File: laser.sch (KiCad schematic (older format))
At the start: 1 part, among them U101 281698-3

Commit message: pushing other ports
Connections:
- net NewBoardCurrentControl/MODULATION_SIGNAL is gone; now on net ArduinoNano/5V_Power_Source: U101.3
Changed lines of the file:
@@
 $EndComp
 Wire Wire Line
-	2950 2550 3000 2550
+	2950 2550 3100 2550
 Wire Wire Line
-	3000 2550 3000 2150
+	3100 2550 3100 3750
 Wire Wire Line
-	3000 2150 10000 2150
+	3100 3750 10000 3750
 Wire Wire Line
-	10000 2150 10000 2800
+	10000 3750 10000 2900
+Connection ~ 10000 2900
+Wire Wire Line
+	10000 2900 10000 2800
 $EndSCHEMATC

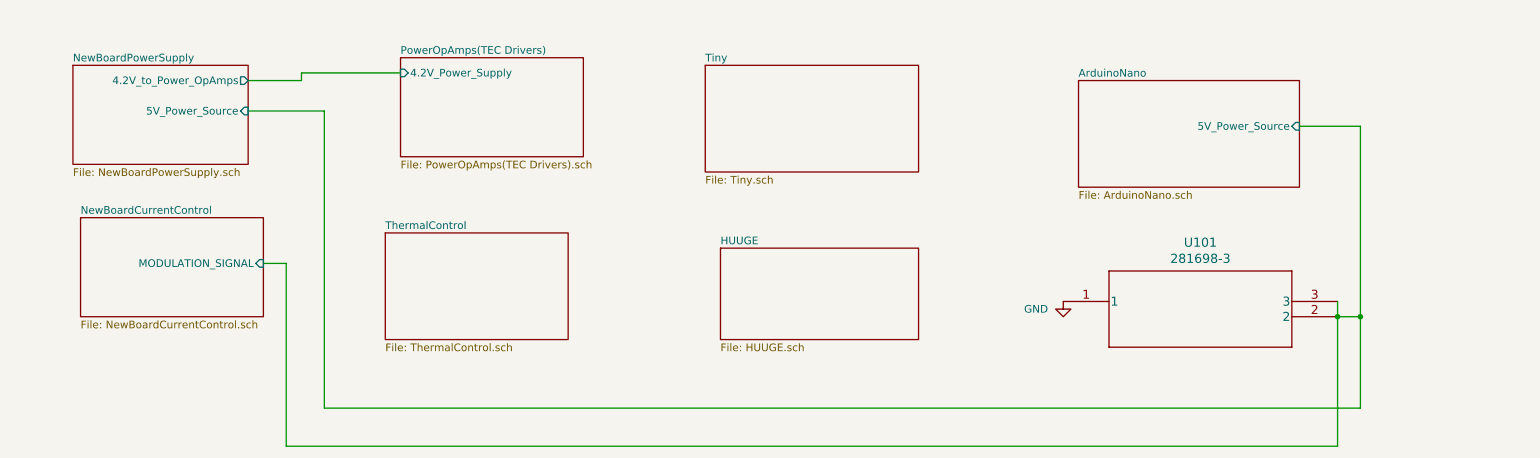
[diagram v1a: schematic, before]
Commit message: added other ports
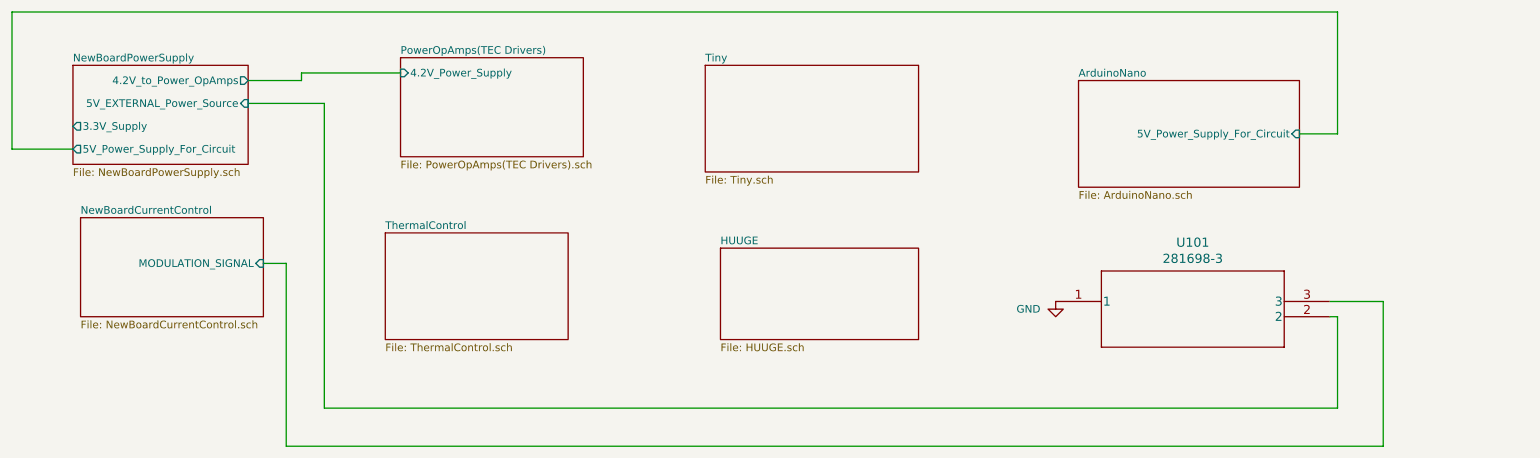
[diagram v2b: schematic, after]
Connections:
- net ArduinoNano/5V_Power_Source renamed NewBoardCurrentControl/MODULATION_SIGNAL
- net NewBoardCurrentControl/MODULATION_SIGNAL: no longer U101.2
- new net NewBoardPowerSupply/5V_EXTERNAL_Power_Source: U101.2
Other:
- moved on the sheet: U101
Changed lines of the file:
@@
 F1 "NewBoardPowerSupply.sch" 50
 F2 "4.2V_to_Power_OpAmps" O R 2850 1350 50
-F3 "5V_Power_Source" I R 2850 1550 50
+F3 "5V_EXTERNAL_Power_Source" I R 2850 1500 50
+F4 "3.3V_Supply" O L 1700 1650 50
+F5 "5V_Power_Supply_For_Circuit" O L 1700 1800 50
 $EndSheet
 $Sheet
@@
 F0 "ArduinoNano" 50
 F1 "ArduinoNano.sch" 50
-F2 "5V_Power_Source" I R 9750 1650 50
+F2 "5V_Power_Supply_For_Circuit" I R 9750 1700 50
 $EndSheet
 Wire Wire Line
@@
 L 3PinHeader:281698-3 U101
 U 1 1 60DB4391
-P 8200 2800
-F 0 "U101" H 9100 3187 60  0000 C CNN
-F 1 "281698-3" H 9100 3081 60  0000 C CNN
-F 2 "footprint libraries:281698-3" H 9100 3040 60  0001 C CNN
-F 3 "" H 8200 2800 60  0000 C CNN
-	1    8200 2800
+P 8150 2800
+F 0 "U101" H 9050 3187 60  0000 C CNN
+F 1 "281698-3" H 9050 3081 60  0000 C CNN
+F 2 "footprint libraries:281698-3" H 9050 3040 60  0001 C CNN
+F 3 "" H 8150 2800 60  0000 C CNN
+	1    8150 2800
 	1    0    0    -1
 $EndComp
 Wire Wire Line
-	2850 1550 3350 1550
+	10000 2900 9950 2900
 Wire Wire Line
-	3350 1550 3350 3500
-Wire Wire Line
-	10150 3500 10150 2900
-Wire Wire Line
-	10150 2900 10000 2900
-Wire Wire Line
-	3350 3500 10150 3500
-Wire Wire Line
-	10150 2900 10150 1650
-Wire Wire Line
-	10150 1650 9750 1650
-Connection ~ 10150 2900
+	3350 3500 10000 3500
 $Comp
 L power:GND #PWR?
 U 1 1 60D4CF8B
-P 8200 2800
-F 0 "#PWR?" H 8200 2550 50  0001 C CNN
-F 1 "GND" H 8100 2750 50  0000 R CNN
-F 2 "" H 8200 2800 50  0001 C CNN
-F 3 "" H 8200 2800 50  0001 C CNN
-	1    8200 2800
+P 8150 2800
+F 0 "#PWR?" H 8150 2550 50  0001 C CNN
+F 1 "GND" H 8050 2750 50  0000 R CNN
+F 2 "" H 8150 2800 50  0001 C CNN
+F 3 "" H 8150 2800 50  0001 C CNN
+	1    8150 2800
 	1    0    0    -1
 $EndComp
@@
 	3100 2550 3100 3750
 Wire Wire Line
-	3100 3750 10000 3750
+	2850 1500 3350 1500
 Wire Wire Line
-	10000 3750 10000 2900
-Connection ~ 10000 2900
+	3350 1500 3350 3500
 Wire Wire Line
-	10000 2900 10000 2800
+	1700 1800 1300 1800
+Wire Wire Line
+	1300 1800 1300 900
+Wire Wire Line
+	1300 900  10000 900
+Wire Wire Line
+	10000 900  10000 1700
+Wire Wire Line
+	9950 2800 10300 2800
+Wire Wire Line
+	10300 2800 10300 3750
+Wire Wire Line
+	3100 3750 10300 3750
+Wire Wire Line
+	10000 3500 10000 2900
+Wire Wire Line
+	9750 1700 10000 1700
 $EndSCHEMATC

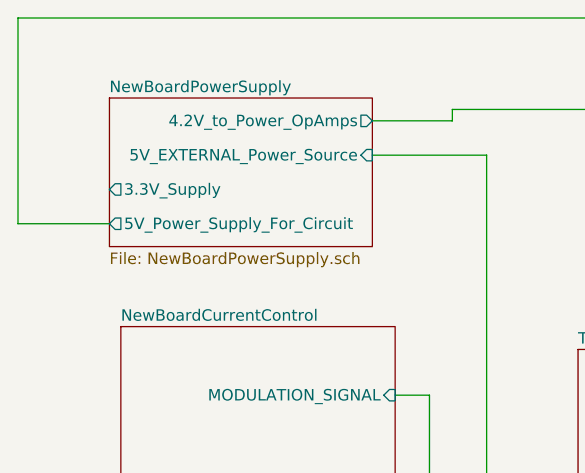
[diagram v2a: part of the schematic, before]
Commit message: added more ports
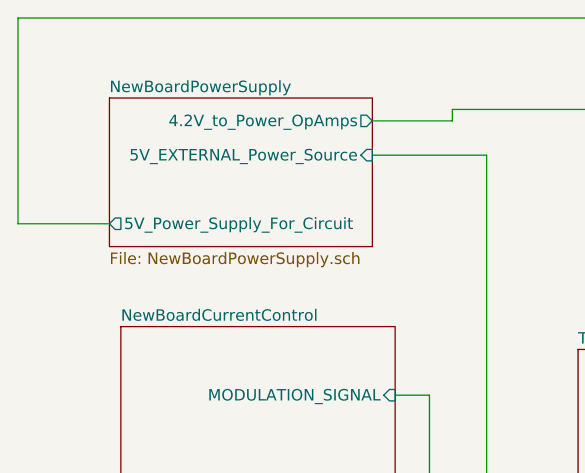
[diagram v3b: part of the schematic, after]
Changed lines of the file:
@@
 F2 "4.2V_to_Power_OpAmps" O R 2850 1350 50
 F3 "5V_EXTERNAL_Power_Source" I R 2850 1500 50
-F4 "3.3V_Supply" O L 1700 1650 50
-F5 "5V_Power_Supply_For_Circuit" O L 1700 1800 50
+F4 "5V_Power_Supply_For_Circuit" O L 1700 1800 50
 $EndSheet
 $Sheet

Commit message: pushing all changes and ports
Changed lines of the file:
@@
 F0 "NewBoardPowerSupply" 50
 F1 "NewBoardPowerSupply.sch" 50
-F2 "4.2V_to_Power_OpAmps" O R 2850 1350 50
-F3 "5V_EXTERNAL_Power_Source" I R 2850 1500 50
-F4 "5V_Power_Supply_For_Circuit" O L 1700 1800 50
+F2 "5V_EXTERNAL_Power_Source" I R 2850 1500 50
 $EndSheet
 $Sheet
@@
 F0 "PowerOpAmps(TEC Drivers)" 50
 F1 "PowerOpAmps(TEC Drivers).sch" 50
-F2 "4.2V_Power_Supply" I L 3850 1300 50
 $EndSheet
 $Sheet
@@
 F0 "ArduinoNano" 50
 F1 "ArduinoNano.sch" 50
-F2 "5V_Power_Supply_For_Circuit" I R 9750 1700 50
 $EndSheet
-Wire Wire Line
-	2850 1350 3200 1350
-Wire Wire Line
-	3200 1350 3200 1300
-Wire Wire Line
-	3200 1300 3850 1300
 $Comp
 L 3PinHeader:281698-3 U101
@@
 	3350 1500 3350 3500
 Wire Wire Line
-	1700 1800 1300 1800
-Wire Wire Line
-	1300 1800 1300 900
-Wire Wire Line
-	1300 900  10000 900
-Wire Wire Line
-	10000 900  10000 1700
-Wire Wire Line
 	9950 2800 10300 2800
 Wire Wire Line
@@
 Wire Wire Line
 	10000 3500 10000 2900
-Wire Wire Line
-	9750 1700 10000 1700
 $EndSCHEMATC

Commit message: name change on main for sheets
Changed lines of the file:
@@
-$EndSheet
-$Sheet
-S 5850 1250 1400 700
-U 60CE0B79
-F0 "Tiny" 50
-F1 "Tiny.sch" 50
-$EndSheet
-$Sheet
-S 5950 2450 1300 600
-U 60CF6290
-F0 "HUUGE" 50
-F1 "HUUGE.sch" 50
 $EndSheet
 $Sheet
@@
 Wire Wire Line
 	10000 3500 10000 2900
+$Sheet
+S 5850 1250 1400 700
+U 60CE0B79
+F0 "Reference" 50
+F1 "Reference.sch" 50
+$EndSheet
+$Sheet
+S 5950 2450 1300 600
+U 60CF6290
+F0 "AtoD_DtoA" 50
+F1 "AtoD_DtoA.sch" 50
+$EndSheet
 $EndSCHEMATC

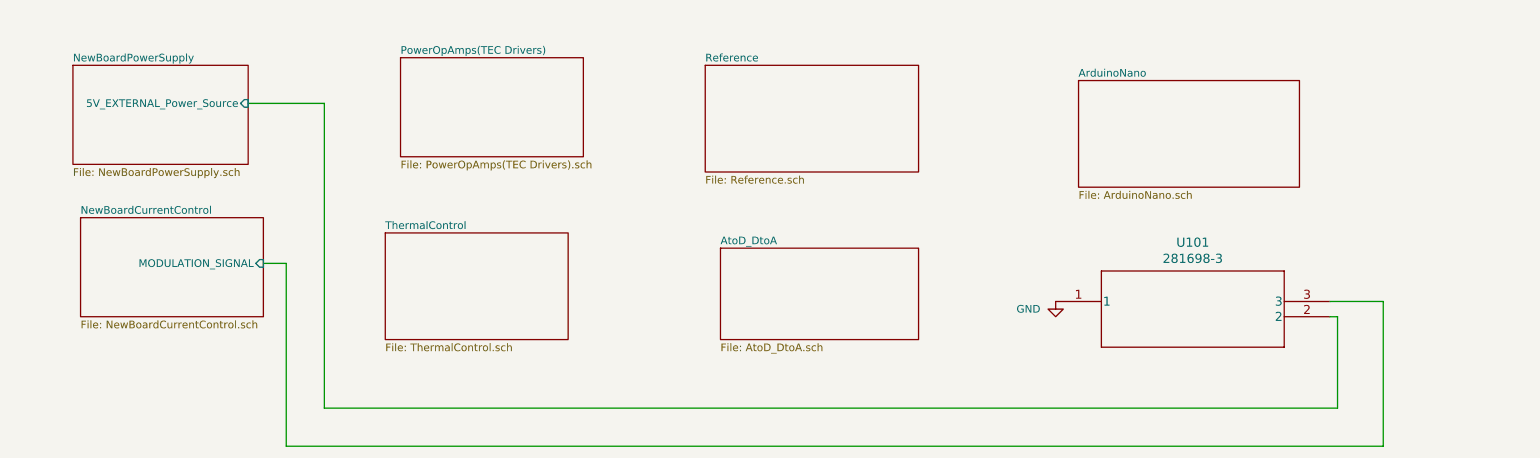
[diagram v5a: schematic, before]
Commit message: replace heirarchal w/ global
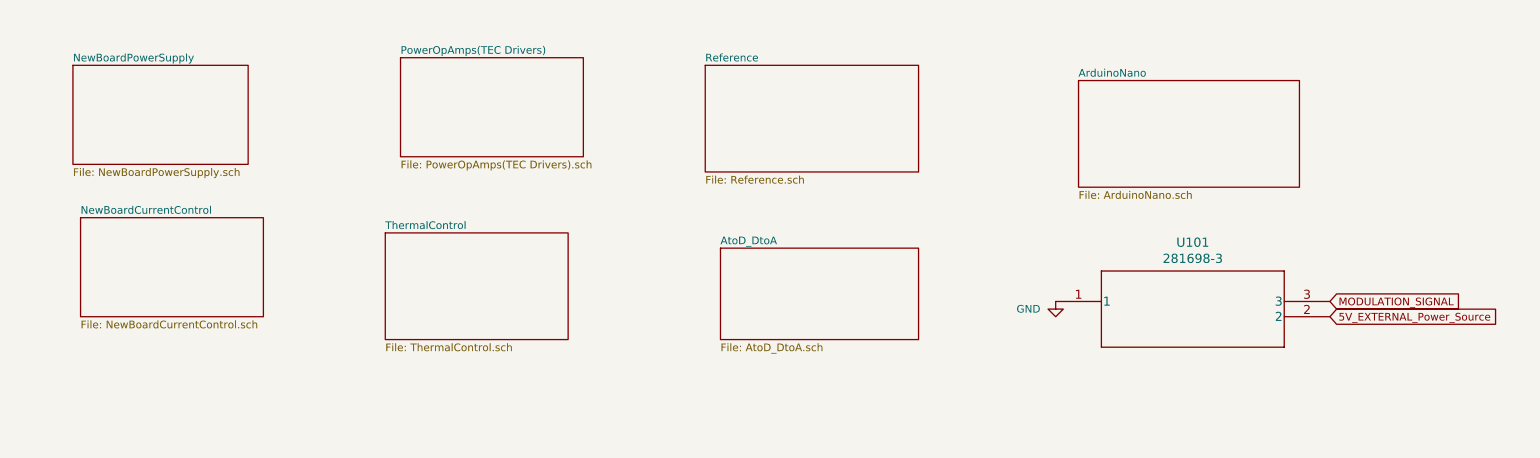
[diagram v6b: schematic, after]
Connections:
- net NewBoardCurrentControl/MODULATION_SIGNAL renamed MODULATION_SIGNAL
- net NewBoardPowerSupply/5V_EXTERNAL_Power_Source renamed 5V_EXTERNAL_Power_Source
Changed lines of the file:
@@
 F0 "NewBoardPowerSupply" 50
 F1 "NewBoardPowerSupply.sch" 50
-F2 "5V_EXTERNAL_Power_Source" I R 2850 1500 50
 $EndSheet
 $Sheet
@@
 F0 "NewBoardCurrentControl" 50
 F1 "NewBoardCurrentControl.sch" 50
-F2 "MODULATION_SIGNAL" I R 2950 2550 50
 $EndSheet
 $Sheet
@@
 	1    0    0    -1
 $EndComp
-Wire Wire Line
-	10000 2900 9950 2900
-Wire Wire Line
-	3350 3500 10000 3500
 $Comp
 L power:GND #PWR?
@@
 	1    0    0    -1
 $EndComp
-Wire Wire Line
-	2950 2550 3100 2550
-Wire Wire Line
-	3100 2550 3100 3750
-Wire Wire Line
-	2850 1500 3350 1500
-Wire Wire Line
-	3350 1500 3350 3500
-Wire Wire Line
-	9950 2800 10300 2800
-Wire Wire Line
-	10300 2800 10300 3750
-Wire Wire Line
-	3100 3750 10300 3750
-Wire Wire Line
-	10000 3500 10000 2900
 $Sheet
 S 5850 1250 1400 700
@@
 F1 "AtoD_DtoA.sch" 50
 $EndSheet
+Text GLabel 9950 2800 2    50   Input ~ 0
+MODULATION_SIGNAL
+Text GLabel 9950 2900 2    50   Input ~ 0
+5V_EXTERNAL_Power_Source
 $EndSCHEMATC
